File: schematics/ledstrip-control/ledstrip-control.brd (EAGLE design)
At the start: 57.5 x 35 mm, 13 parts, among them IC1 LD1117S33CTR, Q3 IRF9530, U1 PHOTON_WITH_HEADERS

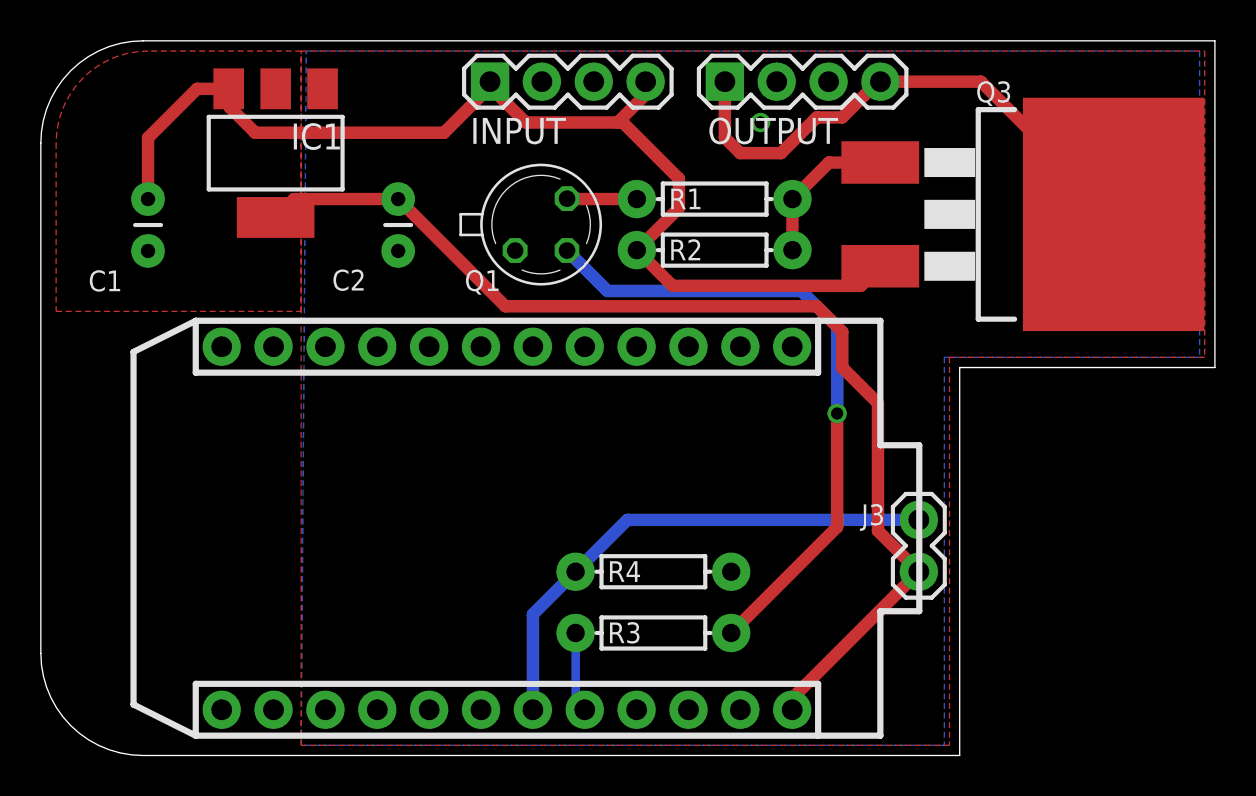
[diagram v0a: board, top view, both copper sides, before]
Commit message: Prepared pcb design for ordering
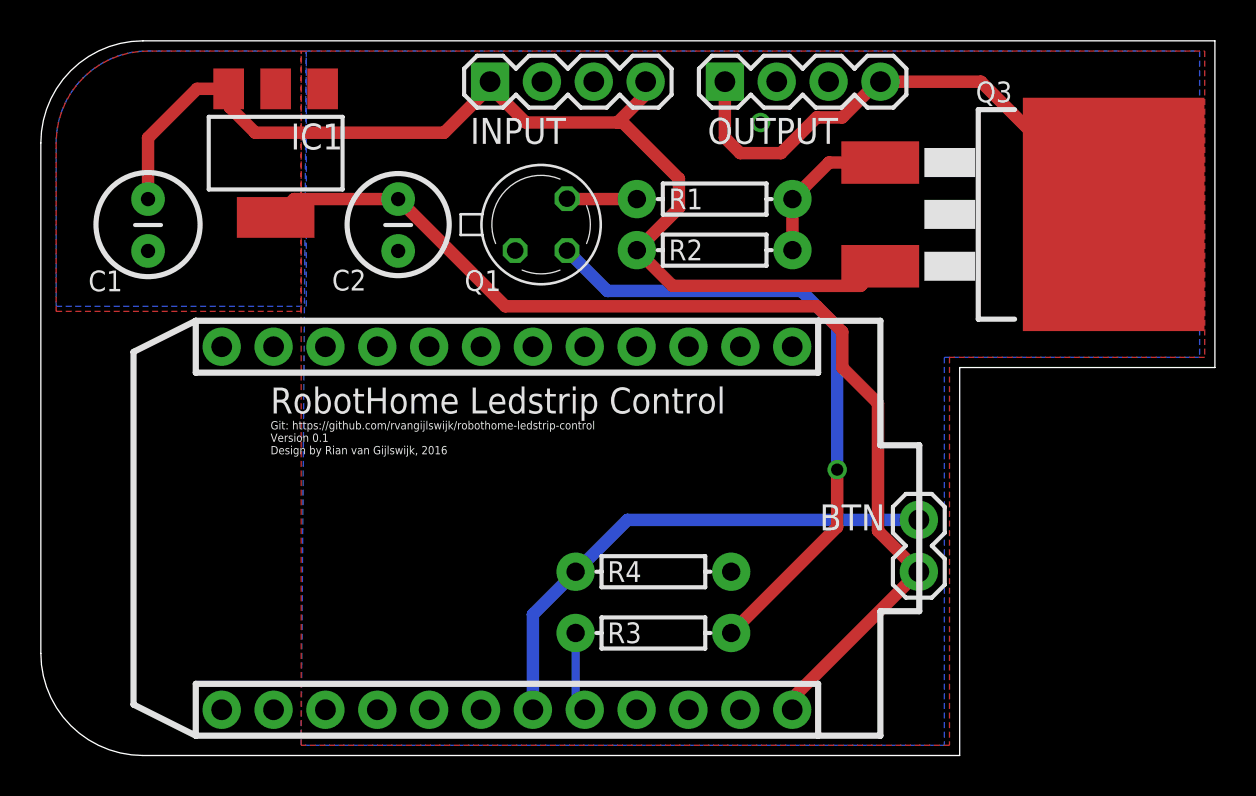
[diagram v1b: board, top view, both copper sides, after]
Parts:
- renumbered J3 to BTN
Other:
- board text added: "BTN"
- board text added: "Git: https://github.com/rvangijlswijk/robothome-ledstrip-control Version 0.1 Design by Rian van Gijlswijk, 2016"
- board text added: "INPUT"
- board text added: "OUTPUT"
- board text added: "RobotHome Ledstrip Control"
- board text removed: "RobotHome - Led Strip Control"
- board text removed: "https://github.com/rvangijlswijk/... version 0.1 commit abc123"
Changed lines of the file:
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@@
 <wire x1="0" y1="30" x2="5" y2="35" width="0" layer="20" curve="-90"/>
 <wire x1="57.5" y1="35" x2="5" y2="35" width="0" layer="20"/>
-<text x="13.12" y="16.75" size="1.27" layer="51" rot="R180" align="top-right">RobotHome - Led Strip Control</text>
-<circle x="5.25" y="26" radius="2.549509375" width="0.254" layer="51"/>
-<circle x="17.5" y="26" radius="2.5" width="0.254" layer="51"/>
+<text x="11.25" y="16.75" size="1.27" layer="25" font="vector" ratio="10" rot="R180" align="top-right">RobotHome Ledstrip Control</text>
+<circle x="5.25" y="26" radius="2.549509375" width="0.254" layer="25"/>
+<circle x="17.5" y="26" radius="2.5" width="0.254" layer="25"/>
 <wire x1="45" y1="0" x2="45" y2="19" width="0" layer="20"/>
 <wire x1="45" y1="19" x2="57.5" y2="19" width="0" layer="20"/>
 <wire x1="57.5" y1="35" x2="57.5" y2="19" width="0" layer="20"/>
-<text x="13.25" y="14.75" size="0.4064" layer="51">https://github.com/rvangijlswijk/...
-version 0.1
-commit abc123</text>
+<text x="11.25" y="14.75" size="0.4064" layer="25" font="vector" ratio="10">Git: https://github.com/rvangijlswijk/robothome-ledstrip-control
+Version 0.1
+Design by Rian van Gijlswijk, 2016</text>
+<text x="30.5" y="30" size="1.27" layer="26" rot="MR0">INPUT</text>
+<text x="42" y="30" size="1.27" layer="26" rot="MR0">OUTPUT</text>
+<text x="41.5" y="11" size="1.27" layer="26" rot="MR0">BTN</text>
 </plain>
 <attributes>
@@
 <attribute name="NAME" x="4" y="23.75" size="1.016" layer="25" rot="R180"/>
 </element>
-<element name="J3" library="SparkFun-Connectors" package="1X02" value="" x="43" y="9" smashed="yes" rot="R90">
-<attribute name="NAME" x="41.3462" y="12.2962" size="1.016" layer="25" ratio="10" rot="R180"/>
+<element name="BTN" library="SparkFun-Connectors" package="1X02" value="" x="43" y="9" smashed="yes" rot="R90">
+<attribute name="NAME" x="41.3462" y="12.2962" size="1.27" layer="25" ratio="10" rot="R180"/>
 <attribute name="VALUE" x="46.175" y="7.73" size="1.27" layer="27" rot="R90"/>
 </element>
@@
 <via x="35.25" y="31" extent="1-16" drill="0.6" shape="square"/>
 <contactref element="IC1" pad="1"/>
+<polygon width="0.254" layer="16">
+<vertex x="13" y="34.5"/>
+<vertex x="5.5" y="34.5" curve="90"/>
+<vertex x="0.75" y="30.25"/>
+<vertex x="0.75" y="22"/>
+<vertex x="13" y="22"/>
+</polygon>
 </signal>
 <signal name="VBAT">
@@
 <signal name="3V3">
 <contactref element="U1" pad="24"/>
-<contactref element="J3" pad="1"/>
+<contactref element="BTN" pad="1"/>
 <contactref element="IC1" pad="4"/>
 <contactref element="C2" pad="1"/>
@@
 <wire x1="27.75" y1="22.75" x2="37.25" y2="22.75" width="0.6096" layer="16"/>
 <wire x1="37.25" y1="22.75" x2="39" y2="21" width="0.6096" layer="16"/>
-<wire x1="39" y1="21" x2="39" y2="16.75" width="0.6096" layer="16"/>
-<via x="39" y="16.75" extent="1-16" drill="0.6" shape="square"/>
-<wire x1="39" y1="16.75" x2="39" y2="11.19" width="0.6096" layer="1"/>
+<wire x1="39" y1="21" x2="39" y2="14" width="0.6096" layer="16"/>
+<via x="39" y="14" extent="1-16" drill="0.6" shape="square"/>
+<wire x1="39" y1="14" x2="39" y2="11.19" width="0.6096" layer="1"/>
 <wire x1="39" y1="11.19" x2="33.81" y2="6" width="0.6096" layer="1"/>
 </signal>
@@
 </signal>
 <signal name="D6">
-<contactref element="J3" pad="2"/>
+<contactref element="BTN" pad="2"/>
 <contactref element="R4" pad="P$1"/>
 <contactref element="U1" pad="19"/>
